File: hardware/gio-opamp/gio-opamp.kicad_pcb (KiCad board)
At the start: 2 copper layers, 19 x 107.5 mm, 55 parts, among them J1 PJ3001F, J2 PJ3001F, J3 oled, J4 eurorack power, J5 PJ3001F, J6 PJ3001F, SW1 encoder, U1 TL072, U2 MCP3208, U3 DAC8552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

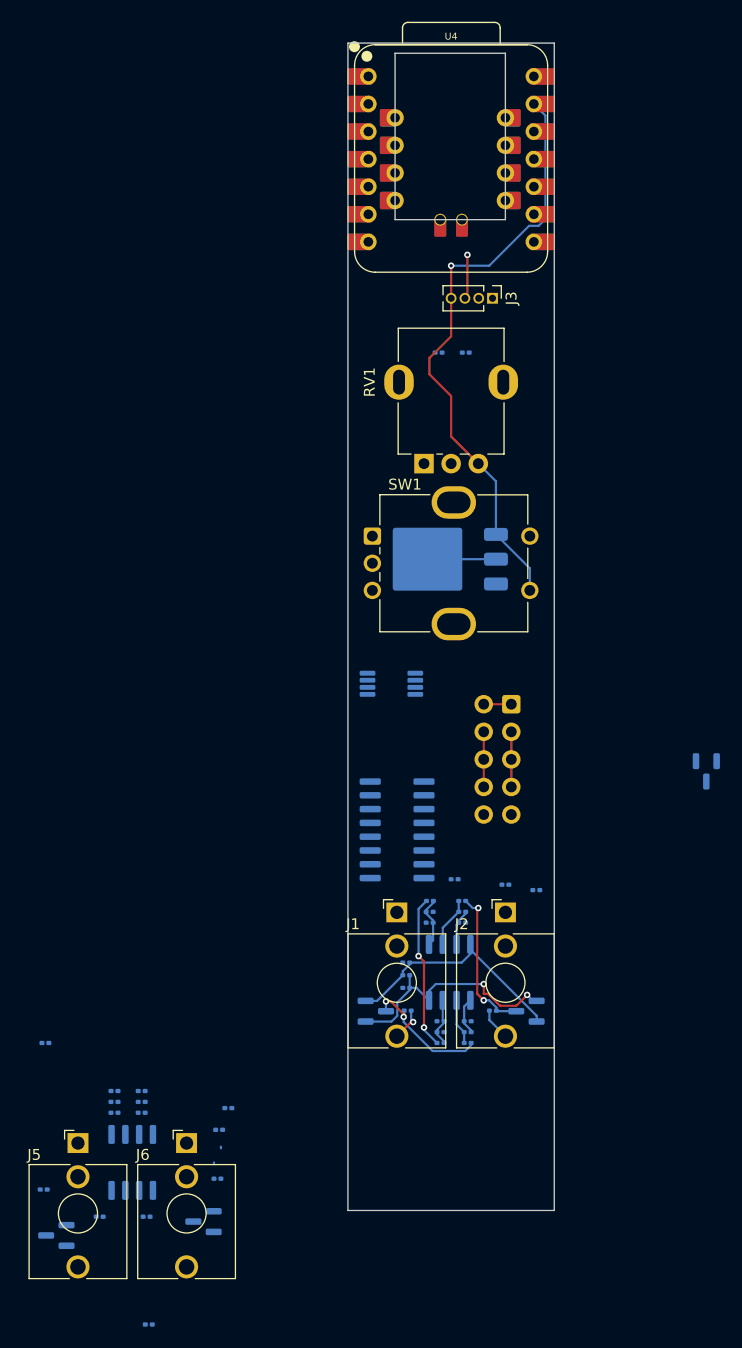
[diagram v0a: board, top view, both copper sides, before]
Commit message: just ratsnest - fresh to route
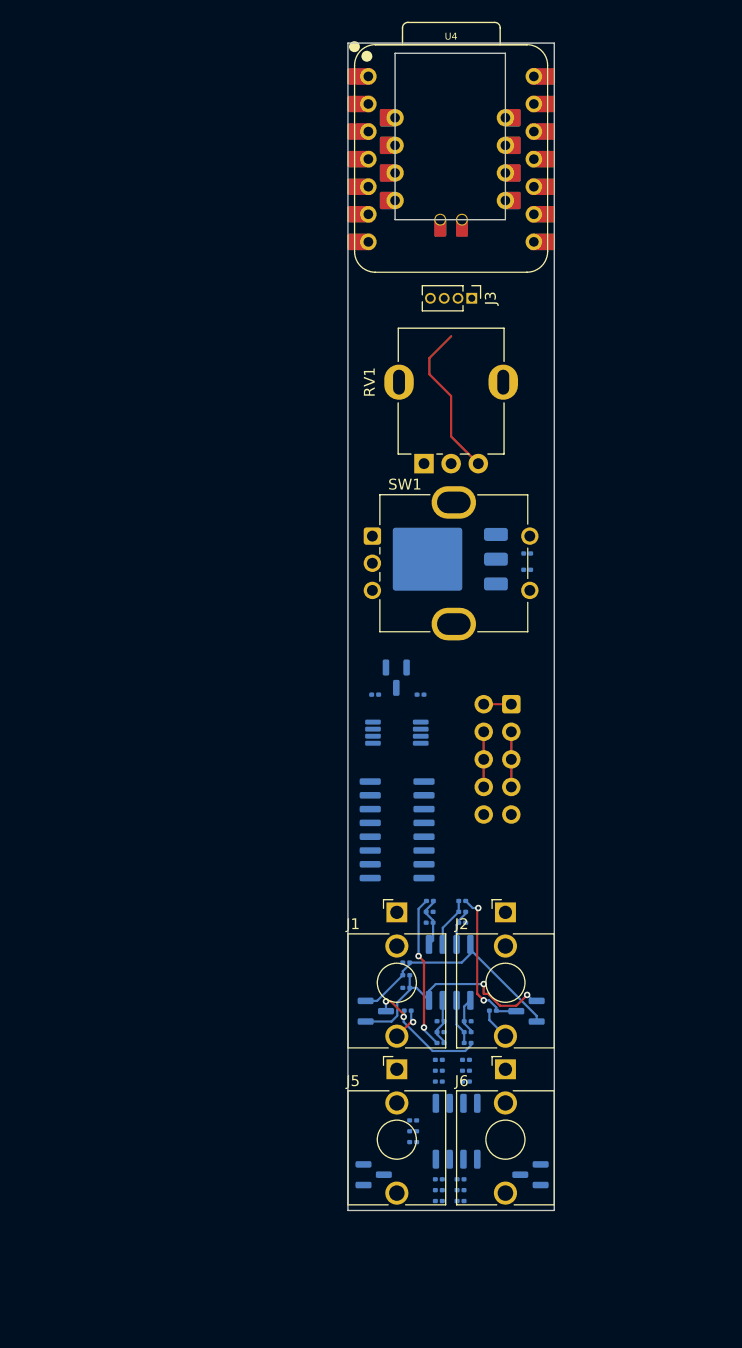
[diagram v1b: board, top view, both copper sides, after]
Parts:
- moved C11 56.7 mm to (48.0, 80.5)
- moved R15 38.4 mm to (41.9, 136.6)
- moved C10 34.8 mm to (37.5, 132.2)
- moved R21 33.3 mm to (41.9, 138.6)
- moved C14 32.0 mm to (34.0, 92.0), turned to 0 degrees
- moved C13 31.8 mm to (38.2, 92.0), turned to 0 degrees
- moved C12 31.0 mm to (48.0, 79.0)
- moved D5 30.4 mm to (48.3, 136.2)
- moved J5 30.1 mm to (36.0, 126.5)
- moved J6 30.1 mm to (46.0, 126.5)
- moved C9 30.0 mm to (39.9, 127.6)
- moved R14 30.0 mm to (42.4, 126.6)
- moved R16 30.0 mm to (42.4, 127.6)
- moved R18 30.0 mm to (39.9, 125.6)
- moved R19 30.0 mm to (39.9, 126.6)
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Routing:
- net GND: track 66.5 -> 24.6 mm, vias 1 -> 0
- net +5V: track 6.30 -> 0.00 mm
- net +3.3V: track 4.10 -> 0.00 mm, vias 1 -> 0
